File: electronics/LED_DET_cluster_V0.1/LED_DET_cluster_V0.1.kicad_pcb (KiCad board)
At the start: 2 copper layers, 15.7 x 15.7 mm, 5 parts, among them J1 Conn_01x06, J2 Conn_01x06, U1 PPG_sensor_PD_4_LED

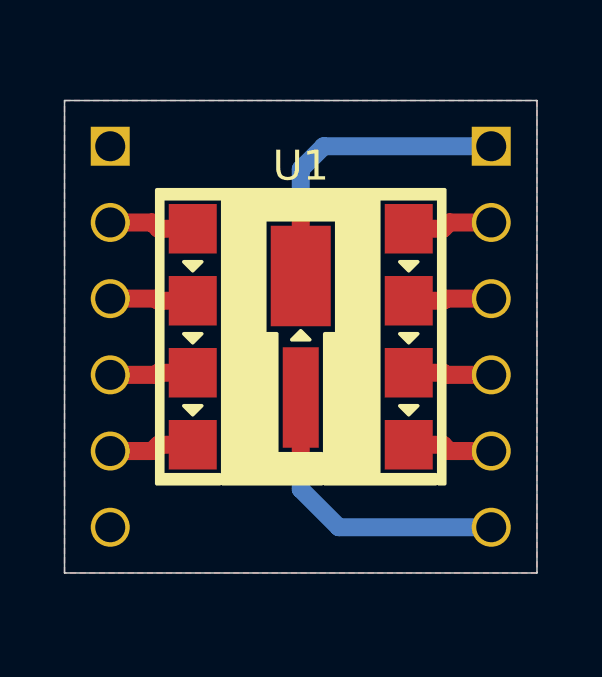
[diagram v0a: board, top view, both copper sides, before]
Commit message: updated PPG LED detector cluster
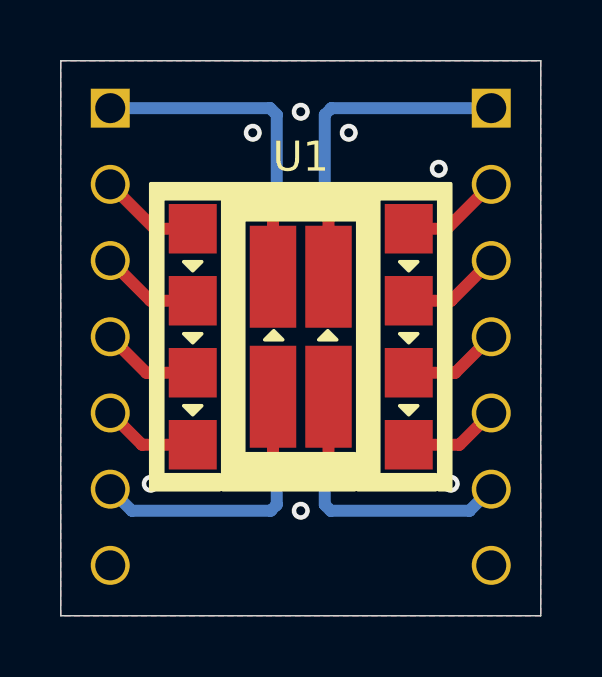
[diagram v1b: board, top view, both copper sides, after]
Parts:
- J1: value Conn_01x06 -> left; footprint SquantorConnectors:Header-0254-1X06-H010 -> SquantorConnectors:Header-0254-1X07-H010
- J2: footprint SquantorConnectors:Header-0254-1X06-H010 -> SquantorConnectors:Header-0254-1X07-H010
- moved N1 1.38 mm to (139.7, 92.4)
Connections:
- J1 pad 1: GND -> /DET2C
- J1 pad 6: GND -> /DET2A
- U1 pad 10: /DET1C -> /LED4A
- U1 pad 5: /DET1A -> /DET2A
- U1 pad 6: /LED3C -> /DET1A
- U1 pad 7: /LED3A -> /LED3C
- U1 pad 8: /LED4C -> /LED3A
- U1 pad 9: /LED4A -> /LED4C
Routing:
- net /DET2C: track 0.00 -> 11.1 mm, vias 0 -> 1
- net /DET2A: track 0.00 -> 9.58 mm, vias 0 -> 1
- net /DET1A: track 10.4 -> 9.58 mm
- net /LED4C: track 2.78 -> 3.31 mm
- net /LED4A: track 2.84 -> 3.36 mm
- net /LED1A: track 2.84 -> 3.36 mm
- net /LED1C: track 2.78 -> 3.31 mm
- net GND: vias 0 -> 7
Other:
- board size 15.7 x 15.7 mm -> 16 x 18.5 mm
